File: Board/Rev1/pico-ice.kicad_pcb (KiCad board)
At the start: 4 copper layers, 22.9 x 61 mm, 109 parts, among them J1 USB_C_Receptacle_USB2.0, J10 2x3_2.54mm_Female, J11 2x3_2.54mm_Female, J2 SWD, J3 6X2 Female Header, J4 6X2 Female Header, J6 6X2 Female Header, J7 6X2 Female Header, J8 6X2 Female Header, J9 BOOT_SEL, SW1 PTS820 J25K SMTR LFS, SW2 PTS820 J25K SMTR LFS, U1 NCP1117ST33T3G, U2 W25Q32JVSSIQ, U3 RP2040, U4 CL9293A12L5M, U5 APS6404L-3SQN-SN, U6 ICE40UP5K-SG48ITR, U8 W25Q32JVSSIQ, Y1 12 MHz

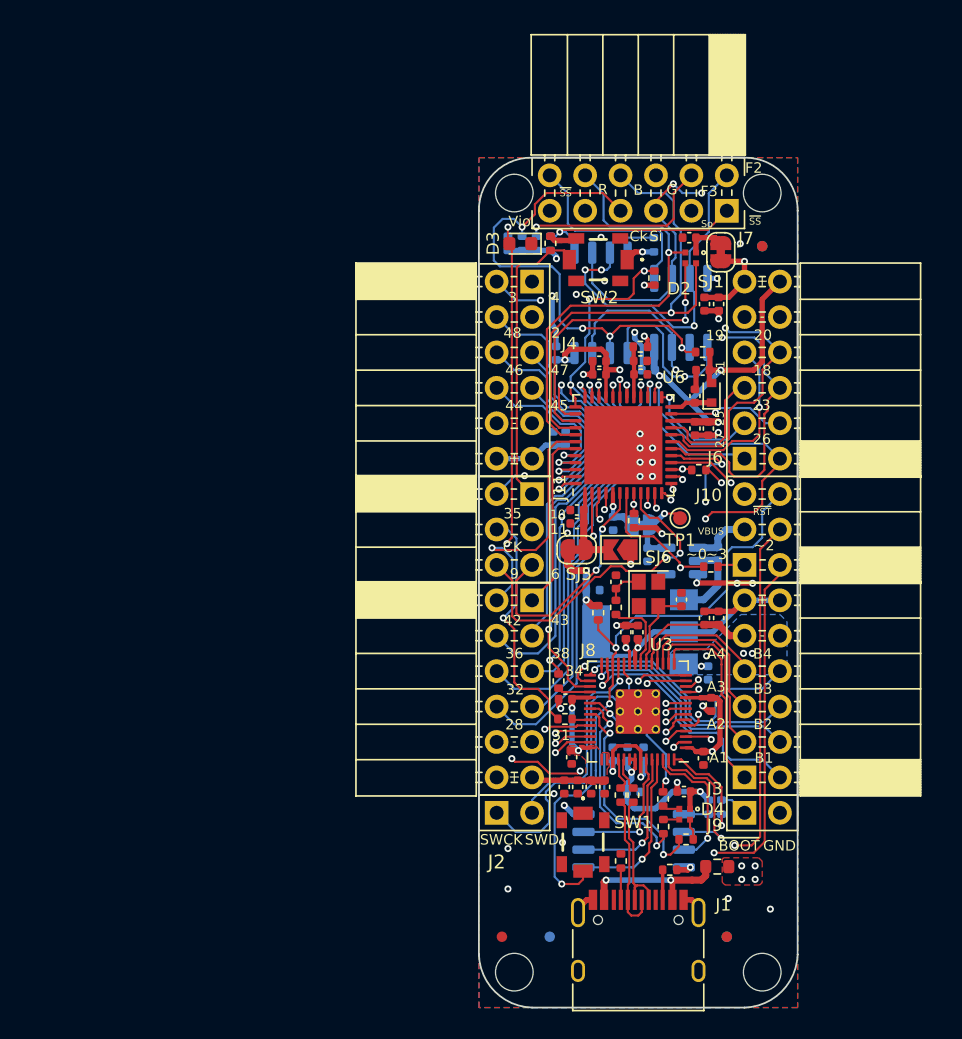
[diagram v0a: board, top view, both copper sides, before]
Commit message: Cleaned up schematic, changed to 2x20 headers
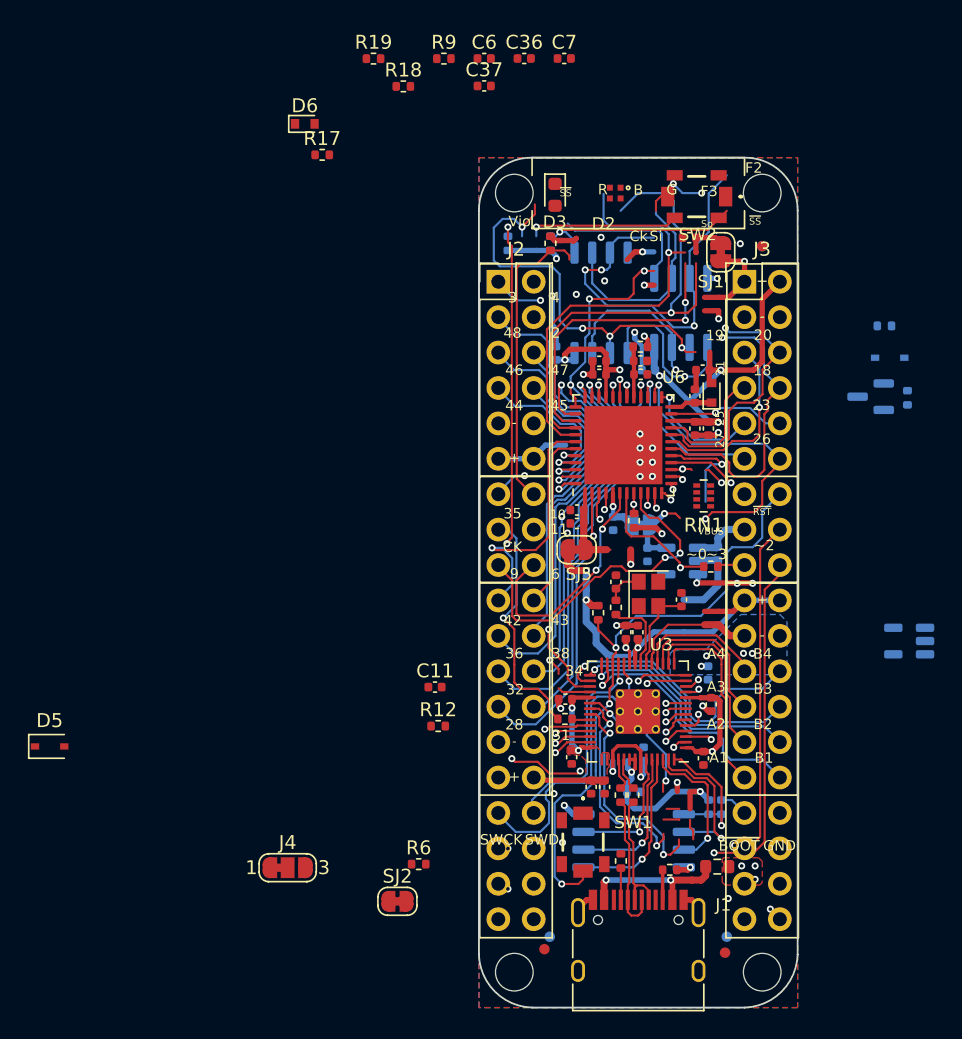
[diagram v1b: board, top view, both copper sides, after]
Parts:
- removed C14, C20, C23, C35, C38, C39, C40, C41: 0.1u, Capacitor_SMD:C_0402_1005Metric
- removed C43: 4.7u, Capacitor_SMD:C_0402_1005Metric
- removed J10, J11: 2x3_2.54mm_Female, Connector_PinSocket_2.54mm:PinSocket_2x03_P2.54mm_Horizontal
- removed J6, J7, J8: 6X2 Female Header, CUSTOM:PMOD_2x06_P2.54mm_Horizontal
- removed J9: BOOT_SEL, Connector_PinHeader_2.54mm:PinHeader_1x02_P2.54mm_Vertical
- removed R20: 2.2K, Resistor_SMD:R_0402_1005Metric
- removed R22: 27, Resistor_SMD:R_0402_1005Metric
- removed SJ6: OPEN, Jumper:SolderJumper-2_P1.3mm_Open_TrianglePad1.0x1.5mm
- removed TP1: TestPoint, TestPoint:TestPoint_Pad_D1.0mm
- added C36: 0.1u, Capacitor_SMD:C_0402_1005Metric, F.Cu at (64.2, 66.5)
- added C37: 4.7u, Capacitor_SMD:C_0402_1005Metric, F.Cu at (61.3, 68.5)
- added D5: 1N5819WS, Diode_SMD:D_SOD-323, F.Cu at (30.2, 115.9)
- added D6: 1N4148WT-7, Diode_SMD:D_SOD-523, F.Cu at (48.5, 71.2)
- added Q1: 2N7002, Package_TO_SOT_SMD:SOT-23, B.Cu at (89.1, 90.8)
- added RN1: 10K, Resistor_SMD:R_Array_Concave_4x0402, F.Cu at (77.1, 97.9)
- added SJ2: SHORT, Jumper:SolderJumper-2_P1.3mm_Bridged_RoundedPad1.0x1.5mm, F.Cu at (55.1, 127.0)
- C11, C6: value 1u -> 4.7u; moved to F.Cu
- C7: moved to F.Cu
- D4: value MHPA1010RGBDT -> 1N5819WS; footprint CUSTOM:LED_Cree-PLCC4_1x1mm_CW -> Diode_SMD:D_SOD-323; moved to B.Cu
- J2: value SWD -> Conn_02x19_Odd_Even; footprint Connector_PinHeader_2.54mm:PinHeader_1x02_P2.54mm_Vertical -> Connector_PinHeader_2.54mm:PinHeader_2x19_P2.54mm_Vertical
- J3: value 6X2 Female Header -> Conn_02x19_Odd_Even; footprint CUSTOM:PMOD_2x06_P2.54mm_Horizontal -> Connector_PinHeader_2.54mm:PinHeader_2x19_P2.54mm_Vertical
- J4: value 6X2 Female Header -> PB_SEL; footprint CUSTOM:PMOD_2x06_P2.54mm_Horizontal -> Jumper:SolderJumper-3_P1.3mm_Bridged12_RoundedPad1.0x1.5mm_NumberLabels
- R12, R9: value 10K -> 27; moved to F.Cu
- R15: value 10K -> 5.1K; moved to B.Cu
- R17: value 10K -> 1k
- R18, R19: value 2.2K -> 1k
- R3: value DNP -> 10K
- R6: value 27 -> 1k
- U1: value NCP1117ST33T3G -> CL9293A12L5M; footprint Package_TO_SOT_SMD:SOT-223-3_TabPin2 -> Package_TO_SOT_SMD:SOT-23-5
- U4: value CL9293A12L5M -> CL9293A33L5M
- moved R19 58.9 mm to (53.4, 66.6), turned to 0 degrees
- moved R18 54.4 mm to (55.5, 68.5), turned to 0 degrees
- moved C6 50.7 mm to (61.3, 66.5), turned to 0 degrees
- moved J4 45.5 mm to (47.2, 124.6)
- moved C7 38.2 mm to (67.1, 66.5)
- moved J2 38.1 mm to (62.4, 82.6), turned to 0 degrees
- moved R12 37.8 mm to (58.0, 114.4), turned to 0 degrees
- moved D4 35.9 mm to (90.4, 88.0), turned to 180 degrees
- moved J3 35.6 mm to (80.0, 82.6), turned to 0 degrees
- moved R17 30.7 mm to (49.7, 73.5)
- moved R13 28.8 mm to (91.7, 90.9), turned to 90 degrees
- moved U1 19.3 mm to (91.8, 108.3)
- moved R15 16.9 mm to (90.0, 85.7), turned to 180 degrees
- moved R6 16.5 mm to (56.6, 124.3), turned to 0 degrees
- moved C11 14.6 mm to (57.8, 111.6), turned to 0 degrees
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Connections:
- C13 pad 1: +1V2 -> +3V3
- C29 pad 1: Net-(C29-Pad1) -> /VIO_BANK_2
- C30 pad 1: Net-(C29-Pad1) -> /VIO_BANK_2
- C42 pad 1: +3V3 -> /+3V3_STDBY
- C7 pad 1: +3V3 -> VBUS
- D2 pad 2: /ICE_LED_B -> Net-(D2-Pad2)
- D2 pad 3: /ICE_LED_G -> Net-(D2-Pad3)
- D2 pad 4: /ICE_LED_R -> Net-(D2-Pad4)
- D4 pad 1: +3V3 -> /+3V3_STDBY
- D4 pad 2: Net-(D4-Pad2) -> +3V3
- J1 pad A4: Net-(J1-PadA4) -> VDC
- J1 pad A9: Net-(J1-PadA4) -> VDC
- J1 pad B4: Net-(J1-PadA4) -> VDC
- J1 pad B9: Net-(J1-PadA4) -> VDC
- J2 pad 1: /SWCLK -> /~{ICE_RST}
- J2 pad 2: /SWD -> /ICE_FLASH_IO2
- PTC1 pad 2: Net-(J1-PadA4) -> Net-(D5-Pad1)
- R12 pad 1: /ICE_FLASH_IO2 -> /ICE_35_G0
- R12 pad 2: +3V3 -> /ICE_CLK
- R13 pad 1: /ICE_FLASH_IO3 -> GND
- R13 pad 2: +3V3 -> /SRAM_SS
- R15 pad 1: /SRAM_SSN -> /+3V3_STDBY
- R15 pad 2: +3V3 -> Net-(Q1-Pad3)
- R17 pad 1: /ICE_SCK -> /LED_R
- R17 pad 2: +3V3 -> Net-(D2-Pad4)
- R18 pad 1: /PICO_LED_R -> /LED_G
- R18 pad 2: Net-(D4-Pad4) -> Net-(D2-Pad3)
- R19 pad 1: /PICO_LED_G -> /LED_B
- R19 pad 2: Net-(D4-Pad3) -> Net-(D2-Pad2)
- R6 pad 1: /ICE_35_G0 -> /PWR_EN
- R6 pad 2: /ICE_CLK -> Net-(C36-Pad1)
- R7 pad 1: /ICE_RSTn -> /~{ICE_RST}
- R7 pad 2: +3V3 -> GND
- R9 pad 2: +3V3 -> Net-(R9-Pad2)
- SJ5 pad 2: Net-(C29-Pad1) -> /VIO_BANK_2
- SW1 pad 2: /~{RESET} -> Net-(J4-Pad2)
- U1 pad 1: GND -> VBUS
- U1 pad 2: +3V3 -> GND
- U1 pad 3: VBUS -> /PWR_EN
- U3 pad 11: /ICE_26 -> /ICE_SO
- U3 pad 12: /ICE_23 -> /ICE_SSN
- U3 pad 13: /ICE_20_G3 -> Net-(R9-Pad2)
- U3 pad 14: /ICE_18 -> /ICE_SI
- U3 pad 15: /PICO_PMOD_A1 -> /LED_G
- U3 pad 16: /PICO_PMOD_A2 -> /LED_R
- U3 pad 17: /PICO_PMOD_A3 -> /SRAM_SS
- U3 pad 18: /PICO_PMOD_A4 -> /LED_B
- U3 pad 2: /ICE_SO -> /ICE_27
- U3 pad 27: /PICO_PMOD_B1 -> /PICO_PMOD_A1
- U3 pad 28: /PICO_PMOD_B2 -> /PICO_PMOD_A2
- U3 pad 29: /PICO_PMOD_B3 -> /PICO_PMOD_A3
- U3 pad 3: /ICE_SSN -> /ICE_25
- U3 pad 30: /PICO_PMOD_B4 -> /PICO_PMOD_A4
- U3 pad 31: /SRAM_SSN -> /PICO_PMOD_B1
- U3 pad 32: /ICE_CLK -> /PICO_PMOD_B2
- U3 pad 34: /PICO_LED_R -> /PICO_PMOD_B3
- U3 pad 35: /PICO_LED_G -> /PICO_PMOD_B4
- U3 pad 36: /PICO_LED_B -> /ICE_CLK
- U3 pad 39: /ICE_RSTn -> /~{ICE_RST}
- U3 pad 4: Net-(R22-Pad2) -> /ICE_21
- U3 pad 40: /ADC2 -> /ADC2|PB
- U3 pad 5: /ICE_SI -> /ICE_19
- U3 pad 6: /ICE_27 -> /ICE_26
- U3 pad 7: /ICE_25 -> /ICE_23
- U3 pad 8: /ICE_21 -> /ICE_20_G3
- U3 pad 9: /ICE_19 -> /ICE_18
- U4 pad 3: VBUS -> Net-(C36-Pad1)
- U4 pad 5: +1V2 -> +3V3
- U5 pad 1: /SRAM_SSN -> Net-(Q1-Pad3)
- U5 pad 8: +3V3 -> /+3V3_STDBY
- U6 pad 1: Net-(C29-Pad1) -> /VIO_BANK_2
- U6 pad 37: /SRAM_SSN -> /SRAM_SS
- U6 pad 39: /ICE_LED_G -> /LED_G
- U6 pad 40: /ICE_LED_B -> /LED_B
- U6 pad 41: /ICE_LED_R -> /LED_R
- U6 pad 8: /ICE_RSTn -> /~{ICE_RST}
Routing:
- net /~{ICE_RST}: track 0.00 -> 70.3 mm, vias 0 -> 2
- net /ICE_RSTn: track 70.3 -> 0.00 mm, vias 2 -> 0
- net /SRAM_SSN: track 56.7 -> 0.00 mm, vias 4 -> 0
- net /LED_G: track 0.00 -> 46.0 mm, vias 0 -> 2
- net /LED_B: track 0.00 -> 44.8 mm, vias 0 -> 1
- net /ADC2|PB: track 0.00 -> 44.3 mm, vias 0 -> 2
- net /ADC2: track 44.3 -> 0.00 mm, vias 2 -> 0
- net /LED_R: track 0.00 -> 43.7 mm, vias 0 -> 1
- net Net-(R9-Pad2): track 0.00 -> 35.9 mm, vias 0 -> 2
- net /ICE_LED_B: track 35.5 -> 0.00 mm, vias 1 -> 0
- net /PICO_PMOD_B1: track 19.1 -> 52.7 mm, vias 1 -> 4
- net /ICE_LED_R: track 33.2 -> 0.00 mm, vias 1 -> 0
- net /ICE_LED_G: track 32.1 -> 0.00 mm, vias 2 -> 0
- net /ICE_27: track 38.3 -> 11.4 mm, vias 2 -> 1
- net Net-(R22-Pad2): track 25.1 -> 0.00 mm, vias 2 -> 0
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
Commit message: Fixed error in PMOD connections to the FPGA, was flipped around: checked that it matches the icebreaker for the dual-dual PMOD & single dual PMOD to the iCE40.
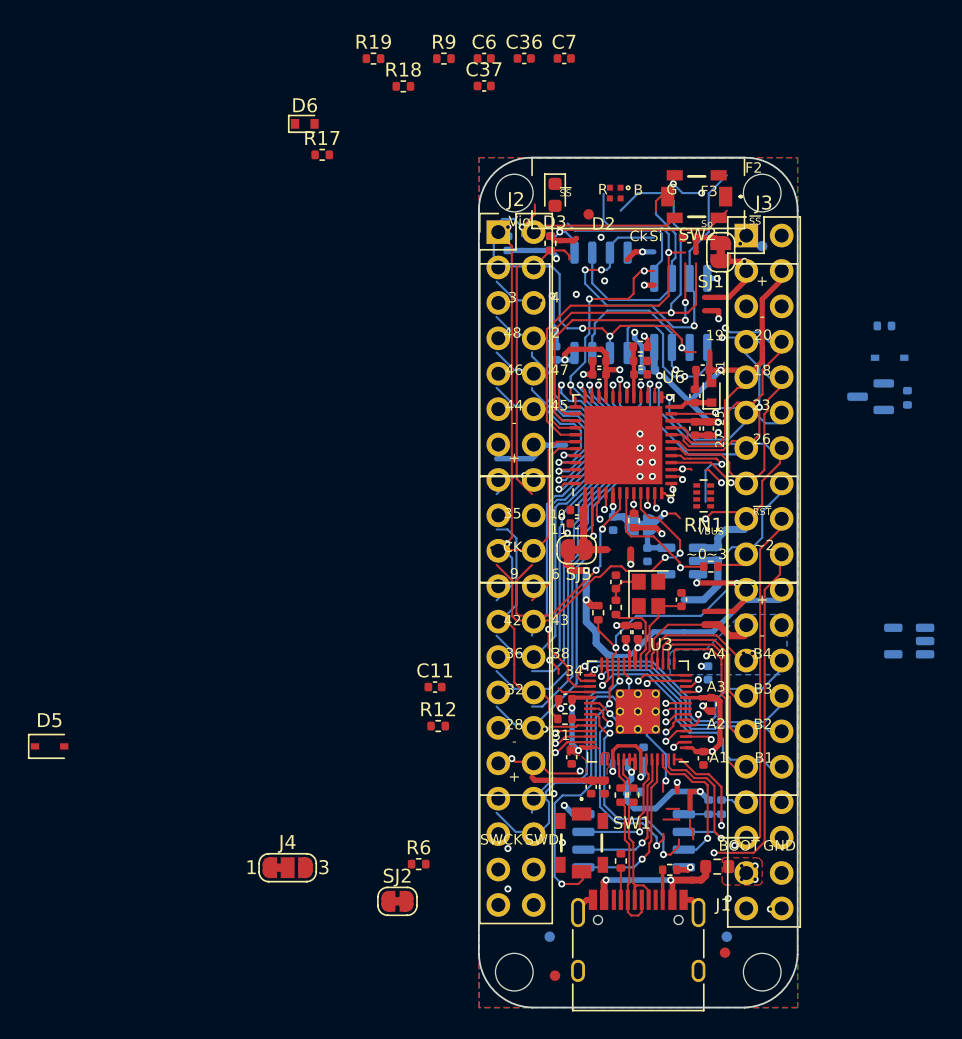
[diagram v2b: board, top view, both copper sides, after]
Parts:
- J2, J3: value Conn_02x19_Odd_Even -> Conn_02x20_Odd_Even; footprint Connector_PinHeader_2.54mm:PinHeader_2x19_P2.54mm_Vertical -> Connector_PinHeader_2.54mm:PinHeader_2x20_P2.54mm_Vertical
- R7: value 10K -> 100K
- moved FID1 12.7 mm to (68.8, 77.7)
- moved J2 3.56 mm to (62.4, 79.0)
- moved J3 3.31 mm to (80.1, 79.2)
- moved FID5 2.05 mm to (66.4, 132.3)
- moved SW1 0.11 mm to (68.3, 122.8)
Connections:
- net +2V5 renamed Net-(U6-Pad24)
- J2 pad 1: /~{ICE_RST} -> /ICE_FLASH_IO2
- J2 pad 10: /ICE_47 -> /ICE_31
- J2 pad 11: /ICE_44_G6 -> /ICE_32
- J2 pad 12: /ICE_45 -> /ICE_34
- J2 pad 13: GND -> /ICE_36
- J2 pad 14: GND -> /ICE_38
- J2 pad 15: /VIO_BANK_2 -> /ICE_42
- J2 pad 16: /VIO_BANK_2 -> /ICE_43
- J2 pad 17: /ICE_10|PB -> /SRAM_SS
- J2 pad 2: /ICE_FLASH_IO2 -> /~{ICE_RST}
- J2 pad 20: /PICO_CLKOUT -> /ICE_6
- J2 pad 21: /ICE_6 -> /ICE_10|PB
- J2 pad 23: /ICE_42 -> /VIO_BANK_2
- J2 pad 24: /ICE_43 -> /VIO_BANK_2
- J2 pad 25: /ICE_36 -> GND
- J2 pad 26: /ICE_38 -> GND
- J2 pad 27: /ICE_32 -> /ICE_44_G6
- J2 pad 28: /ICE_34 -> /ICE_45
- J2 pad 29: /ICE_28 -> /ICE_46
- J2 pad 3: /SRAM_SS -> /ICE_FLASH_IO3
- J2 pad 30: /ICE_31 -> /ICE_47
- J2 pad 31: GND -> /ICE_48
- J2 pad 32: GND -> /ICE_2
- J2 pad 33: +3V3 -> /ICE_3
- J2 pad 34: +3V3 -> /ICE_4
- J2 pad 36: /SWCLK -> /~{RESET}
- J2 pad 37: /PWR_EN -> /SWCLK
- J2 pad 38: /+3V3_STDBY -> GND
- J2 pad 4: /ICE_FLASH_IO3 -> GND
- J2 pad 5: /ICE_3 -> +3V3
- J2 pad 6: /ICE_4 -> +3V3
- J2 pad 7: /ICE_48 -> GND
- J2 pad 8: /ICE_2 -> GND
- J2 pad 9: /ICE_46 -> /ICE_28
- J3 pad 10: GND -> /ICE_20_G3
- J3 pad 12: /ICE_20_G3 -> /ICE_18
- J3 pad 13: /ICE_21 -> GND
- J3 pad 14: /ICE_18 -> GND
- J3 pad 15: /ICE_25 -> +3V3
- J3 pad 16: /ICE_23 -> +3V3
- J3 pad 17: /ICE_27 -> /ICE_DONE_ADC0
- J3 pad 18: /ICE_26 -> /LED_B
- J3 pad 19: VDC -> /ADC2|PB
- J3 pad 2: /LED_R -> /ICE_SO
- J3 pad 20: /~{RESET} -> /LED_R
- J3 pad 21: VBUS -> /ADC3
- J3 pad 22: /ADC2|PB -> /LED_G
- J3 pad 23: /ICE_DONE_ADC0 -> /PICO_PMOD_A1
- J3 pad 24: /ADC3 -> /PICO_PMOD_B1
- J3 pad 25: +3V3 -> /PICO_PMOD_A2
- J3 pad 26: +3V3 -> /PICO_PMOD_B2
- J3 pad 27: GND -> /PICO_PMOD_A3
- J3 pad 28: GND -> /PICO_PMOD_B3
- J3 pad 3: /ICE_SO -> /ICE_SI
- J3 pad 31: /PICO_PMOD_A3 -> GND
- J3 pad 32: /PICO_PMOD_B3 -> GND
- J3 pad 33: /PICO_PMOD_A2 -> +3V3
- J3 pad 34: /PICO_PMOD_B2 -> +3V3
- J3 pad 35: /PICO_PMOD_A1 -> /PWR_EN
- J3 pad 36: /PICO_PMOD_B1 -> +3V3
- J3 pad 37: /~{USB_BOOT} -> VDC
- J3 pad 38: GND -> /+3V3_STDBY
- J3 pad 4: /LED_G -> /ICE_SCK
- J3 pad 5: /ICE_SCK -> /ICE_27
- J3 pad 6: /LED_B -> /ICE_26
- J3 pad 7: +3V3 -> /ICE_25
- J3 pad 8: +3V3 -> /ICE_23
- J3 pad 9: GND -> /ICE_21
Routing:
- net GND: track 52.3 -> 470.3 mm, vias 31 -> 52
- net /~{ICE_RST}: track 70.3 -> 479.0 mm, vias 2 -> 26
- net /ICE_DONE: track 76.2 -> 0.00 mm, vias 5 -> 0
- net /ICE_SI: track 91.1 -> 15.0 mm, vias 5 -> 0
- net +3V3: track 140.2 -> 214.1 mm, vias 20 -> 26
- net /ICE_25: track 57.3 -> 0.00 mm, vias 3 -> 0
- net /PICO_PMOD_B1: track 52.7 -> 0.00 mm, vias 4 -> 0
- net /ICE_6: track 17.3 -> 66.8 mm, vias 2 -> 5
- net /ICE_DONE_ADC0: track 46.4 -> 0.00 mm, vias 1 -> 0
- net /ADC2|PB: track 44.3 -> 0.00 mm, vias 2 -> 0
- net /~{RESET}: track 44.0 -> 0.00 mm, vias 3 -> 0
- net /ICE_18: track 43.7 -> 0.00 mm, vias 1 -> 0
- net /ADC3: track 42.2 -> 0.00 mm, vias 2 -> 0
- net /SRAM_SS: track 10.8 -> 52.7 mm, vias 0 -> 4
- net /ICE_20_G3: track 41.8 -> 0.00 mm, vias 1 -> 0
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
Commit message: Update pico-ice.kicad_pcb
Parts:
- C36, C37, C7, D6, R6, SJ2: moved to B.Cu
- R14: moved to F.Cu
- moved R9 48.0 mm to (77.6, 110.6), turned to -90 degrees
- moved D5 47.7 mm to (77.1, 124.7), turned to 180 degrees
- moved D6 42.5 mm to (76.4, 103.3), turned to 180 degrees
- moved C6 42.2 mm to (70.6, 107.7), turned to 90 degrees
- moved C7 40.8 mm to (72.1, 107.1), turned to 180 degrees
- moved C36 38.7 mm to (74.9, 103.8), turned to -90 degrees
- moved C37 35.2 mm to (72.1, 102.0), turned to 180 degrees
- moved SJ2 29.7 mm to (76.3, 106.2), turned to 180 degrees
- moved R6 26.9 mm to (74.0, 103.8), turned to 90 degrees
- moved D3 25.8 mm to (75.5, 100.5), turned to 90 degrees
- moved R14 25.1 mm to (77.1, 100.6), turned to 0 degrees
- moved R13 23.1 mm to (73.5, 76.7), turned to -90 degrees
- moved R19 21.1 mm to (72.2, 76.1), turned to -90 degrees
- moved U1 20.5 mm to (71.6, 104.5), turned to 90 degrees
- moved R17 19.7 mm to (69.3, 76.1), turned to 90 degrees
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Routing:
- net +3V3: track 214.1 -> 171.5 mm, vias 26 -> 21
- net +1V2: track 0.00 -> 19.3 mm, vias 0 -> 2
- net /ICE_SSN: track 15.6 -> 1.26 mm, vias 1 -> 0
- net /~{ICE_RST}: track 479.0 -> 466.7 mm
- net /LED_B: track 35.5 -> 24.0 mm
- net /LED_R: track 31.4 -> 21.2 mm, vias 1 -> 0
- net /SRAM_SS: track 52.7 -> 43.2 mm
- net GND: track 470.3 -> 463.1 mm, vias 52 -> 43
- net /ICE_FLASH_IO2: track 44.6 -> 38.2 mm
- net /ICE_6: track 66.8 -> 61.0 mm, vias 5 -> 4
- net /ICE_9: track 12.9 -> 15.5 mm
- net /PICO_PMOD_B2: track 2.37 -> 0.00 mm
- net VDC: track 10.9 -> 9.11 mm
- net /+3V3_STDBY: track 0.00 -> 1.66 mm
- net /ICE_27: track 0.00 -> 1.02 mm
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- removed copper zone on F.Cu, net VBUS

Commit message: Finished the placement for a review.
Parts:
- added R20: DNI, Resistor_SMD:R_0603_1608Metric_Pad0.98x0.95mm_HandSolder, F.Cu at (74.2, 123.3)
- added R22: DNI, Resistor_SMD:R_0603_1608Metric_Pad0.98x0.95mm_HandSolder, F.Cu at (74.2, 122.0)
- C3: moved to F.Cu
- R10, R24: footprint Resistor_SMD:R_0402_1005Metric -> Resistor_SMD:R_0603_1608Metric_Pad0.98x0.95mm_HandSolder
- moved FID2 23.4 mm to (58.4, 75.2)
- moved FID4 22.8 mm to (56.2, 126.0)
- moved FID3 20.9 mm to (57.7, 129.1)
- moved LOGO2 20.7 mm to (95.8, 119.9)
- moved FID1 11.2 mm to (58.4, 73.6)
- moved FID6 10.8 mm to (55.3, 128.6)
- moved R21 10.5 mm to (76.6, 79.6), turned to 0 degrees
- moved PTC1 9.88 mm to (77.1, 120.8), turned to -90 degrees
- moved C3 8.13 mm to (77.1, 118.7), turned to 0 degrees
- moved FID5 7.82 mm to (58.6, 132.2)
- moved R10 4.01 mm to (74.2, 120.8)
- moved R19 3.63 mm to (69.3, 78.3), turned to 90 degrees
- moved C32 3.10 mm to (73.2, 78.3), turned to 0 degrees
- moved R24 3.08 mm to (74.2, 124.6), turned to 0 degrees
- moved R17 3.07 mm to (71.5, 78.3)
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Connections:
- J3 pad 24: /PICO_PMOD_B1 -> unconnected-(J3-Pad24)
- J3 pad 26: /PICO_PMOD_B2 -> unconnected-(J3-Pad26)
- J3 pad 28: /PICO_PMOD_B3 -> unconnected-(J3-Pad28)
- J3 pad 30: /PICO_PMOD_B4 -> unconnected-(J3-Pad30)
- J3 pad 35: /PWR_EN -> +3V3
- J3 pad 36: +3V3 -> VDC
- J3 pad 37: VDC -> /+3V3_STDBY
- J3 pad 38: /+3V3_STDBY -> /PWR_EN
- J3 pad 39: GND -> VBUS
- J3 pad 40: VBUS -> GND
- R10 pad 1: Net-(J1-PadB5) -> Net-(J1-PadA5)
- R17 pad 2: Net-(D2-Pad4) -> Net-(D2-Pad2)
- R19 pad 2: Net-(D2-Pad2) -> Net-(D2-Pad4)
- R24 pad 1: Net-(J1-PadA5) -> Net-(J1-PadB5)
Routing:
- net /~{ICE_RST}: track 466.7 -> 0.00 mm, vias 26 -> 0
- net +3V3: track 171.5 -> 617.5 mm, vias 21 -> 42
- net /ICE_6: track 61.0 -> 0.00 mm, vias 4 -> 0
- net /ADC3: track 0.00 -> 55.2 mm, vias 0 -> 5
- net /PICO_CLKOUT: track 0.00 -> 46.9 mm, vias 0 -> 2
- net unconnected-(J3-Pad30): track 0.00 -> 46.2 mm, vias 0 -> 2
- net /PICO_PMOD_A4: track 46.2 -> 0.00 mm, vias 2 -> 0
- net Net-(Q1-Pad3): track 0.00 -> 43.0 mm, vias 0 -> 4
- net /SRAM_SS: track 43.2 -> 0.25 mm, vias 4 -> 0
- net unconnected-(J3-Pad26): track 0.00 -> 31.5 mm, vias 0 -> 1
- net /PICO_PMOD_A3: track 31.5 -> 0.00 mm, vias 1 -> 0
- net /ICE_31: track 28.3 -> 57.9 mm, vias 1 -> 3
- net /ICE_46: track 29.6 -> 0.00 mm, vias 2 -> 0
- net /~{RESET}: track 0.00 -> 25.3 mm, vias 0 -> 3
- net /ICE_3: track 25.1 -> 0.00 mm, vias 2 -> 0
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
